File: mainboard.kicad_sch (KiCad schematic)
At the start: 21 parts, among them J1 USB_C_Receptacle_USB2.0_16P, J10 Valve7, J11 AuxPump, J12 MainPump, J13 WaterLevelSensor, J14 OneWireTemp, J15 OneWireTemp, J17 FlowSensor, J2 Valve1, J3 Servo, J4 HX711, J5 Valve2, J6 Valve3, J7 Valve4, J8 Valve5, J9 Valve6

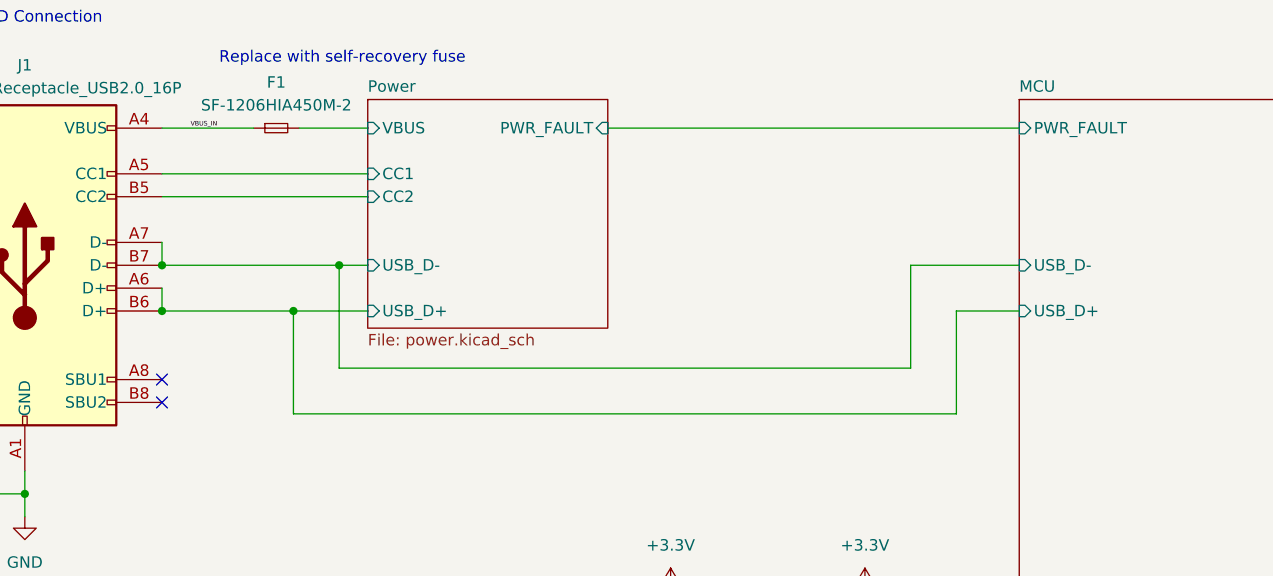
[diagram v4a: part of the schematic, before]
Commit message: Improve USB ESD connection
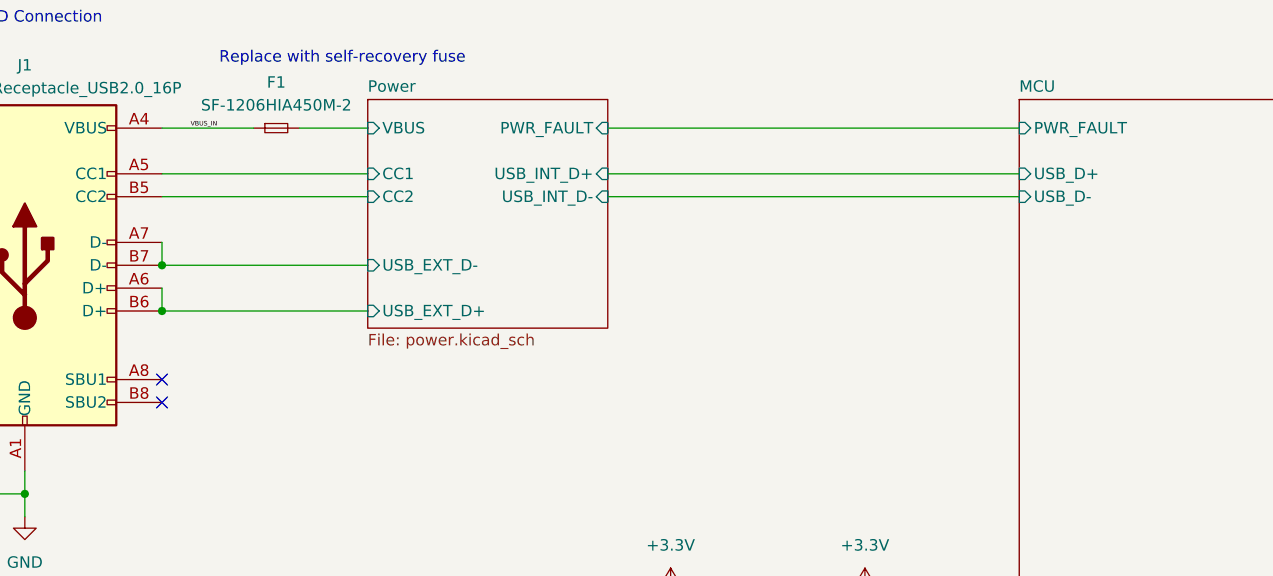
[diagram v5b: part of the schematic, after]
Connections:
- net MCU/USB_D+: no longer J1.A6 (D+), J1.B6 (D+)
- net MCU/USB_D-: no longer J1.A7 (D-), J1.B7 (D-)
- new net Power/USB_EXT_D+: J1.A6 (D+), J1.B6 (D+)
- new net Power/USB_EXT_D-: J1.A7 (D-), J1.B7 (D-)
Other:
- sheet Power ports: added USB_EXT_D+, USB_EXT_D-, USB_INT_D+, USB_INT_D-; removed USB_D+, USB_D-
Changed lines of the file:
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@@
   (junction (at 81.915 97.155) (diameter 0) (color 0 0 0 0)
   )
-  (junction (at 101.6 92.075) (diameter 0) (color 0 0 0 0)
-  )
   (junction (at 337.82 64.77) (diameter 0) (color 0 0 0 0)
   )
@@
   )
   (junction (at 81.915 92.075) (diameter 0) (color 0 0 0 0)
-  )
-  (junction (at 96.52 97.155) (diameter 0) (color 0 0 0 0)
   )
   (junction (at 337.82 73.66) (diameter 0) (color 0 0 0 0)
@@
     (stroke (width 0) (type default))
   )
-  (wire (pts (xy 101.6 103.505) (xy 101.6 92.075))
-    (stroke (width 0) (type default))
-  )
   (wire (pts (xy 59.055 114.935) (xy 59.055 117.475))
     (stroke (width 0) (type default))
@@
     (stroke (width 0) (type default))
   )
-  (wire (pts (xy 170.18 108.585) (xy 96.52 108.585))
-    (stroke (width 0) (type default))
-  )
   (wire (pts (xy 319.405 153.035) (xy 340.36 153.035))
     (stroke (width 0) (type default))
@@
     (stroke (width 0) (type default))
   )
-  (wire (pts (xy 177.165 97.155) (xy 170.18 97.155))
-    (stroke (width 0) (type default))
-  )
   (wire (pts (xy 329.565 67.31) (xy 359.41 67.31))
     (stroke (width 0) (type default))
@@
     (stroke (width 0) (type default))
   )
-  (wire (pts (xy 170.18 97.155) (xy 170.18 108.585))
-    (stroke (width 0) (type default))
-  )
-  (wire (pts (xy 165.1 103.505) (xy 101.6 103.505))
-    (stroke (width 0) (type default))
-  )
   (wire (pts (xy 332.74 76.2) (xy 359.41 76.2))
     (stroke (width 0) (type default))
@@
     (stroke (width 0) (type default))
   )
-  (wire (pts (xy 165.1 92.075) (xy 165.1 103.505))
-    (stroke (width 0) (type default))
-  )
   (wire (pts (xy 160.02 140.97) (xy 160.02 139.065))
     (stroke (width 0) (type default))
@@
     (stroke (width 0) (type default))
   )
-  (wire (pts (xy 96.52 108.585) (xy 96.52 97.155))
+  (wire (pts (xy 131.445 81.915) (xy 177.165 81.915))
     (stroke (width 0) (type default))
   )
@@
     (stroke (width 0) (type default))
   )
-  (wire (pts (xy 96.52 97.155) (xy 104.775 97.155))
+  (wire (pts (xy 81.915 97.155) (xy 104.775 97.155))
     (stroke (width 0) (type default))
   )
@@
     (stroke (width 0) (type default))
   )
-  (wire (pts (xy 81.915 92.075) (xy 101.6 92.075))
-    (stroke (width 0) (type default))
-  )
   (wire (pts (xy 319.405 96.52) (xy 326.39 96.52))
     (stroke (width 0) (type default))
@@
     (stroke (width 0) (type default))
   )
-  (wire (pts (xy 101.6 92.075) (xy 104.775 92.075))
+  (wire (pts (xy 81.915 92.075) (xy 104.775 92.075))
     (stroke (width 0) (type default))
   )
@@
     (stroke (width 0) (type default))
   )
-  (wire (pts (xy 81.915 97.155) (xy 96.52 97.155))
-    (stroke (width 0) (type default))
-  )
   (wire (pts (xy 275.59 124.46) (xy 273.05 124.46))
     (stroke (width 0) (type default))
@@
     (stroke (width 0) (type default))
   )
+  (wire (pts (xy 131.445 84.455) (xy 177.165 84.455))
+    (stroke (width 0) (type default))
+  )
   (wire (pts (xy 266.7 144.78) (xy 272.415 144.78))
     (stroke (width 0) (type default))
@@
   )
   (wire (pts (xy 329.565 77.47) (xy 329.565 67.31))
-    (stroke (width 0) (type default))
-  )
-  (wire (pts (xy 177.165 92.075) (xy 165.1 92.075))
     (stroke (width 0) (type default))
   )
@@
       (effects (font (size 1.27 1.27)) (justify right))
     )
-    (pin "USB_D-" input (at 104.775 92.075 180)
-      (effects (font (size 1.27 1.27)) (justify left))
-    )
-    (pin "USB_D+" input (at 104.775 97.155 180)
-      (effects (font (size 1.27 1.27)) (justify left))
+    (pin "USB_EXT_D-" input (at 104.775 92.075 180)
+      (effects (font (size 1.27 1.27)) (justify left))
+    )
+    (pin "USB_EXT_D+" input (at 104.775 97.155 180)
+      (effects (font (size 1.27 1.27)) (justify left))
+    )
+    (pin "USB_INT_D+" input (at 131.445 81.915 0)
+      (effects (font (size 1.27 1.27)) (justify right))
+    )
+    (pin "USB_INT_D-" input (at 131.445 84.455 0)
+      (effects (font (size 1.27 1.27)) (justify right))
     )
     (instances
@@
       (effects (font (size 1.27 1.27)) (justify left top))
     )
-    (pin "USB_D-" input (at 177.165 92.075 180)
-      (effects (font (size 1.27 1.27)) (justify left))
-    )
-    (pin "USB_D+" input (at 177.165 97.155 180)
-      (effects (font (size 1.27 1.27)) (justify left))
-    )
     (pin "VALVE3_CTRL" input (at 222.885 85.09 0)
       (effects (font (size 1.27 1.27)) (justify right))
@@
       (effects (font (size 1.27 1.27)) (justify right))
     )
-    (instances
+    (pin "USB_D-" input (at 177.165 84.455 180)
+      (effects (font (size 1.27 1.27)) (justify left))
+    )
+    (pin "USB_D+" input (at 177.165 81.915 180)
+      (effects (font (size 1.27 1.27)) (justify left))
+    )
+    (instances

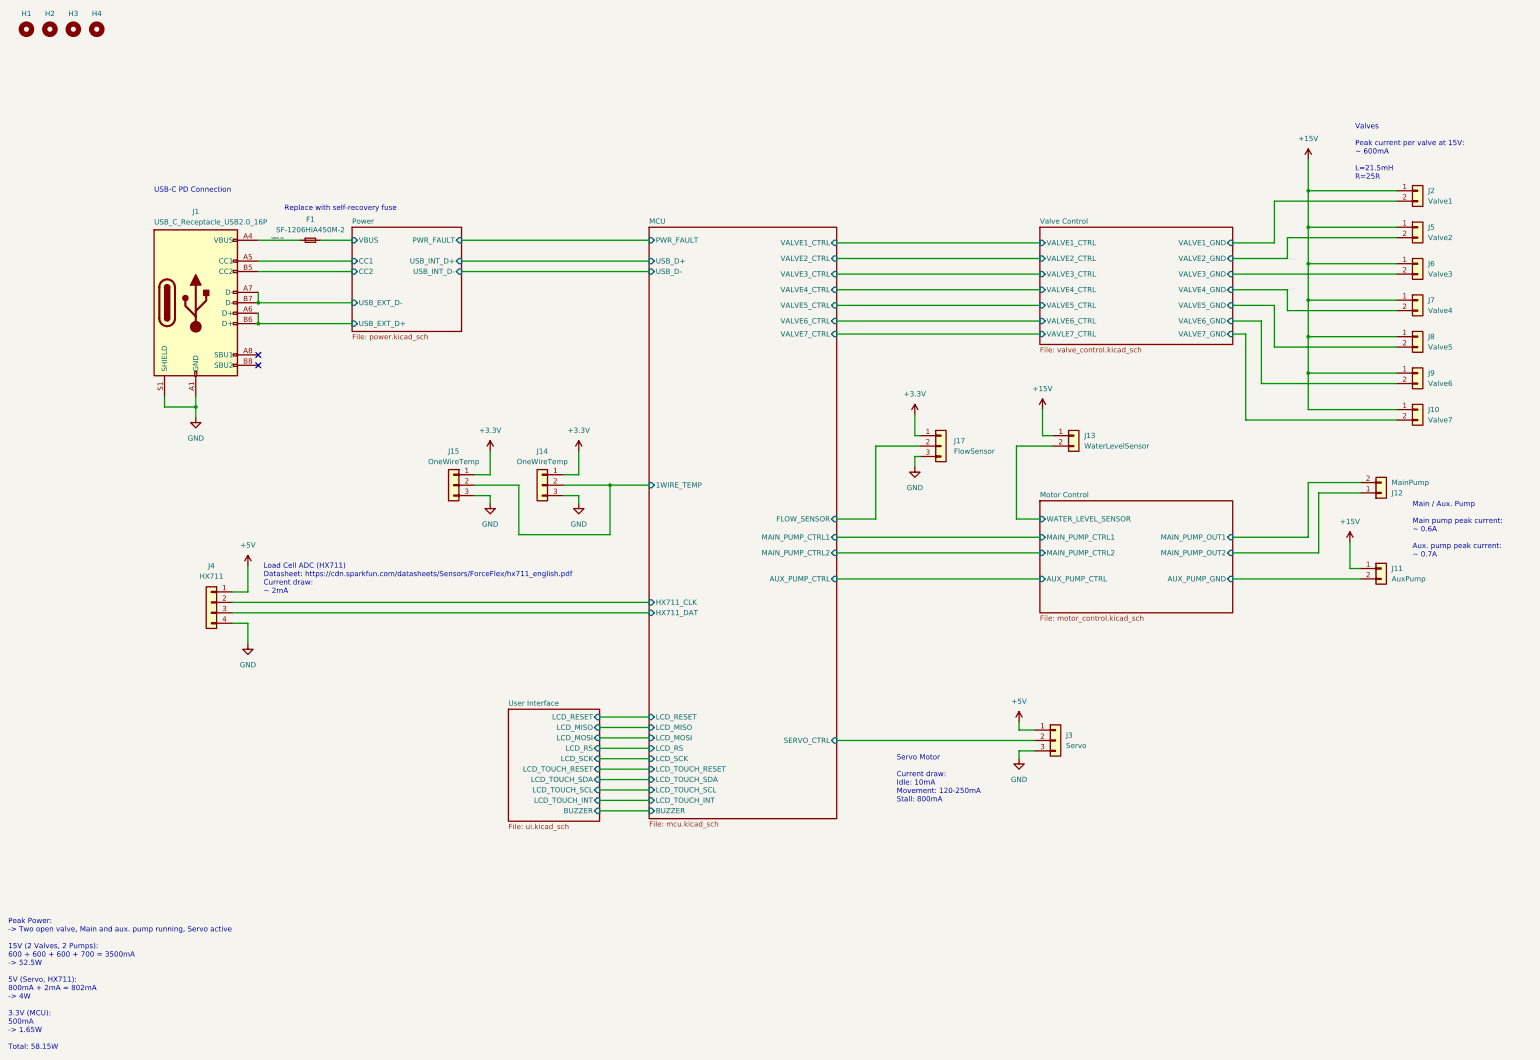
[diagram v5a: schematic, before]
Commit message: Re-annotate parts by board
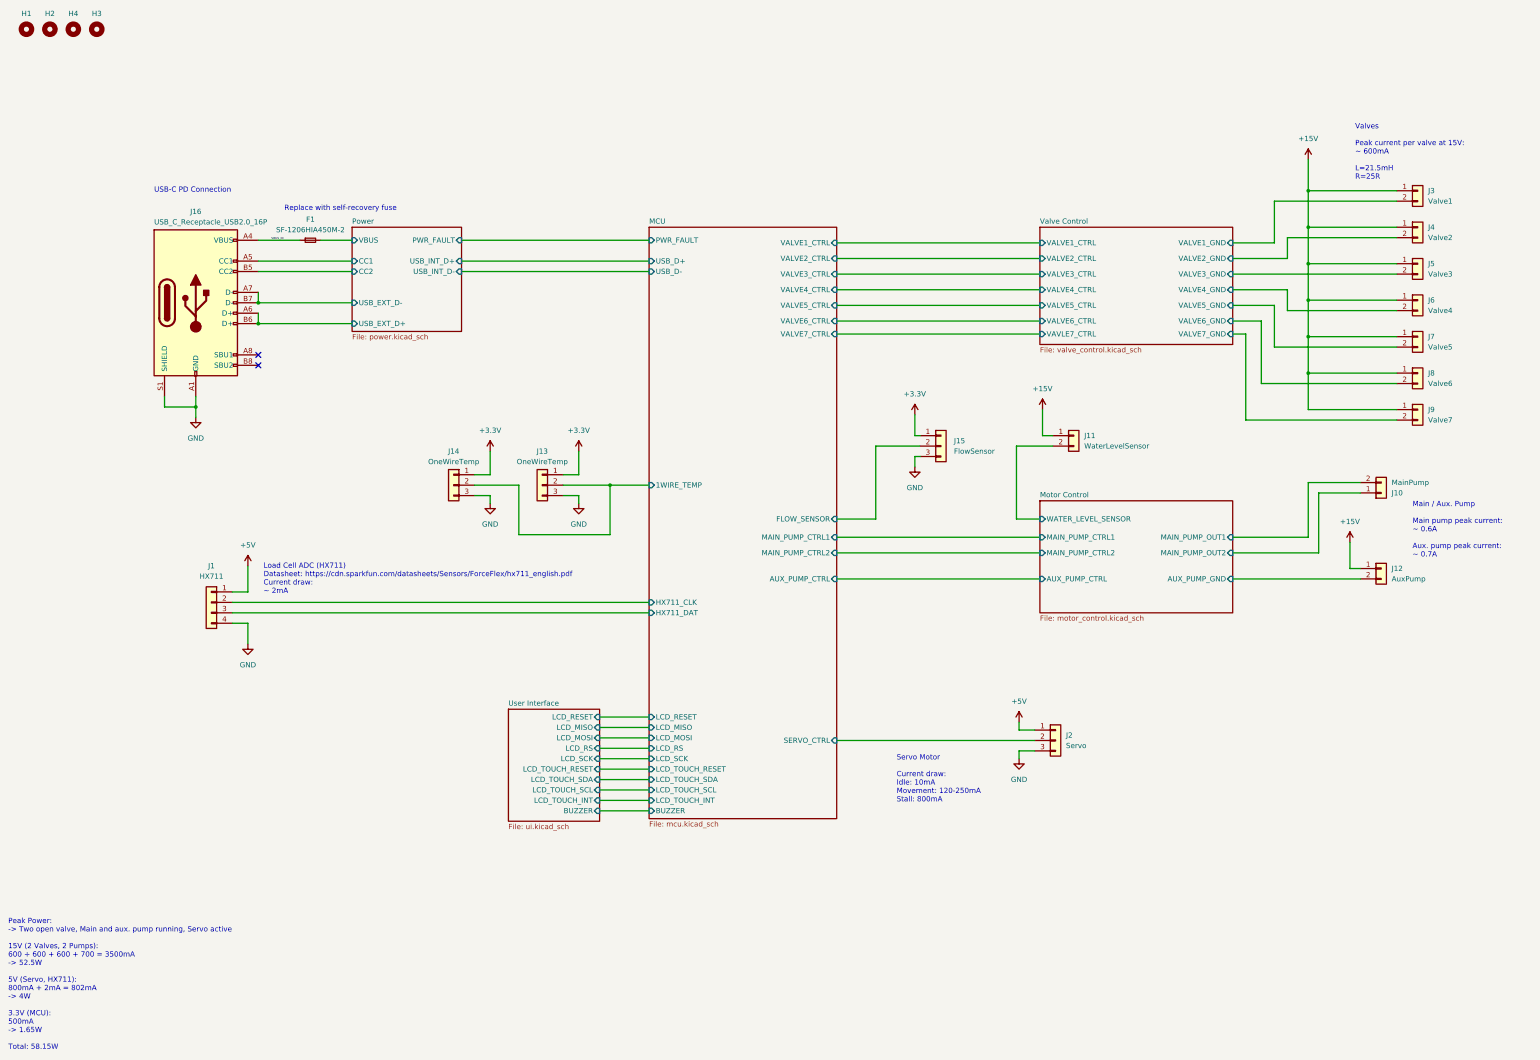
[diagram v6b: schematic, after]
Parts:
- renumbered H4 to H3, H3 to H4, J4 to J1, J12 to J10, J13 to J11, J11 to J12, J14 to J13, J15 to J14, J17 to J15, J1 to J16, J3 to J2, J2 to J3, J5 to J4, J6 to J5, J7 to J6, J8 to J7, J9 to J8, J10 to J9

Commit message: Redesign power rails to use barrel jack 12V input
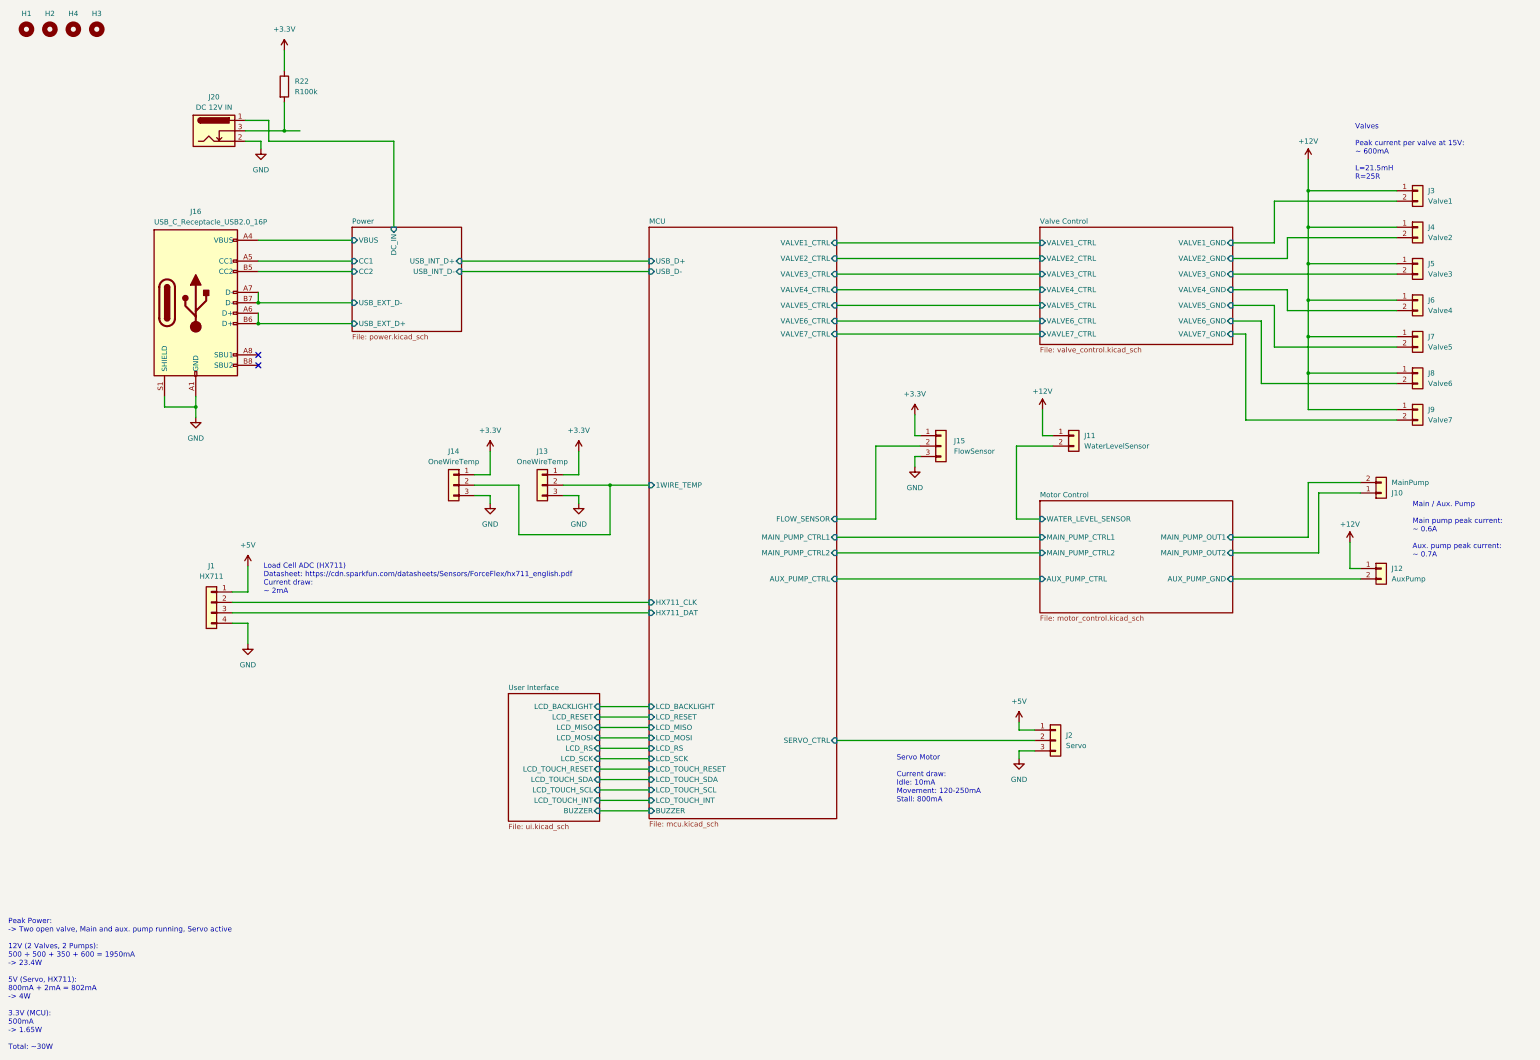
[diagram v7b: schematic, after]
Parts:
- removed F1: SF-1206HIA450M-2, Fuse:Fuse_1206_3216Metric, symbol Device:Fuse_Small
- added J20: DC 12V IN, Connector_BarrelJack:BarrelJack_Wuerth_6941xx301002, symbol Connector:Barrel_Jack_Switch
- added R22: R100k, Resistor_SMD:R_0805_2012Metric, symbol Device:R
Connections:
- net VBUS_IN is gone; now on net Power/VBUS: J16.A4 (VBUS), J16.A9 (VBUS), J16.B4 (VBUS), J16.B9 (VBUS)
- net +3.3V: now also R22.1
- net GND: now also J20.2
- net +15V renamed +12V
- new net: J20.3, R22.2
- new net Power/DC_IN: J20.1
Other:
- sheet MCU ports: added LCD_BACKLIGHT; removed PWR_FAULT
- sheet Power ports: added DC_IN; removed PWR_FAULT
- sheet User Interface ports: added LCD_BACKLIGHT; removed none
- note added: "Peak Power: -> Two open valve, Main and aux. pump running, Servo active 12V (2 Valves, 2 Pumps): 500 + 500 + 350 + 600 = 1950mA -> 23.4W 5V (Servo, HX711): 800mA + 2mA = 802mA -> 4W 3.3V (MCU): 500mA -> 1.65W Total: ~30W"
- note removed: "Peak Power: -> Two open valve, Main and aux. pump running, Servo active 15V (2 Valves, 2 Pumps): 600 + 600 + 600 + 700 = 3500mA -> 52.5W 5V (Servo, HX711): 800mA + 2mA = 802mA -> 4W 3.3V (MCU): 500mA -> 1.65W Total: 58.15W"
- note removed: "Replace with self-recovery fuse"
- note removed: "USB-C PD Connection"
